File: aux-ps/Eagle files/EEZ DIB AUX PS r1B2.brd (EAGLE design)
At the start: 210 x 60 mm, 116 parts, among them IC1 AMC6821SDBQR, IC2 VIPer35L, IC3 TL431, J1 PF0030/PC, J2 1-726388-2, J3 1-726388-2, J4 1-726388-2, J5 SWEB 8094 AU/GN, Q1 BTA26-600, Q2 BTA26-600, Q3 2N7002, Q4 2N7002, Q5 BSP716NH6327XTSA1, Q6 2N7002, SW1 DF62J12S2AHQA, X1 39-28-1063, X2 39-30-1039, X3 ZL231-16KG, X4 22-23-2031, X5 22-23-2021

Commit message: r1B2 changes
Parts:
- removed LED2: LTST-C170YKT, EEZ_Lib1:LED_0805
- added R35: 1K8, rcl:R0805
- added R36: 47K, rcl:R0805
- added R37: 4K7, rcl:R0805
- C13, C19: device rcl:C1206 -> rcl:C1210
- C20: value *** -> N.C.
- C23: value 10n -> 3n3
- R11: value 2K2 -> 330R/2W; device rcl:R0805 -> rcl:R2512
- R12: value 10K -> 47K
- R13: value 470R -> 2K2
- R14, R33: value 47K -> 10K
- R15: value 10K -> 470R
- R16: value 4K7 -> 47K
- R17: value 220K -> 10K; device rcl:R1206 -> rcl:R0805
- R18: value 220K -> 4K7; device rcl:R1206 -> rcl:R0805
- R19, R21: value 120R -> 220K; device rcl:R0805 -> rcl:R1206
- R20: value 100K -> 220K; device rcl:R0805 -> rcl:R1206
- R22: value 22R -> 120R
- R23: value 120R -> 100K
- R24: value 470R -> 120R
- R25, R28: value *** -> 1K
- R26: value N.C. -> 22R
- R27: value 24K -> 120R
- R29: value 47K -> N.C.
- R30: value 47K -> 4K7
- R31: value 12K -> 10K
- R32: value 1K8 -> 47K
- R34: value 4K7 -> 6K8
- R6: value 49R9 -> 47K
- R7: value 220R -> 330R/2W; device rcl:R0805 -> rcl:R2512
- R8: value 330R/2W -> 49R9; device rcl:R2512 -> rcl:R0805
- R9: value 330R/2W -> 220R; device rcl:R2512 -> rcl:R0805
- moved R24 107.0 mm to (113.7, 54.3), turned to 270 degrees
- moved R11 99.2 mm to (137.4, 6.10), turned to 270 degrees
- moved R6 77.6 mm to (71.8, 52.2), turned to 90 degrees
- moved R14 67.4 mm to (103.8, 55.0), turned to 270 degrees
- moved R22 59.3 mm to (62.4, 38.0), turned to 90 degrees
- moved R17 58.9 mm to (49.4, 43.9)
- moved R33 58.3 mm to (65.7, 18.4), turned to 0 degrees
- moved R18 57.9 mm to (47.4, 43.9), turned to 90 degrees
- moved R34 55.2 mm to (115.3, 38.4), turned to 180 degrees
- moved R9 52.0 mm to (145.2, 58.0), turned to 180 degrees
- moved R23 50.8 mm to (110.2, 44.3), turned to 0 degrees
- moved R31 45.7 mm to (74.9, 17.1), turned to 270 degrees
- moved R19 44.3 mm to (105.3, 26.7)
- moved R12 32.0 mm to (71.8, 56.1), turned to 90 degrees
- moved R27 21.2 mm to (62.4, 29.1), turned to 270 degrees
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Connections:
- removed net N$10: LED2.C, R24.1
- removed net N$63: C3.1, C4.1, D1.C, L1.1, R12.2, X4.1
- new net +12V_FAN: C3.1, C4.1, D1.C, L1.1, R14.2, X4.1
- net +12V_REC: now also R22.1, R25.1; no longer R19.1
- net +3V3: now also R13.1; no longer R11.1
- net +5V: now also R16.1, R30.2; no longer LED2.A, R14.1, R27.2
- net +5V_REC: now also R27.1; no longer R23.1
- net 0V: now also R34.1, R35.2, R36.2; no longer R31.1, R32.2, R33.2
- net AC_N_OUT: now also R11.1; no longer R9.1
- net AC_OUT_L: now also R7.2; no longer R8.2
- net AUX: now also R29.2; no longer R26.2
- net AUX_OUT: now also R26.2; no longer R22.2
- net AUX_REC: now also R24.1, R26.1; no longer R21.1, R22.1
- net DC_BUS: now also R19.1, R20.1, R21.1; no longer R17.1, R18.1
- net FAN_SENSE: now also R14.1, R17.2; no longer R12.1, R15.2
- net FB1: now also R31.2; no longer R28.2
- net GND: now also R12.1, R18.2, R25.2, R37.1, R6.1; no longer R16.2, R24.2, R34.1
- net N$12: now also R28.1; no longer R25.1
- net N$13: now also R15.2; no longer R13.2
- net N$137: now also R19.2, R20.2; no longer R17.2
- net N$14: now also R15.1; no longer R13.1
- net N$140: now also R24.2; no longer R21.2
- net N$141: now also R32.1, R34.2; no longer R26.1, R31.2
- net N$146: now also R27.2; no longer R23.2
- net N$148: now also R30.1, R33.2, R37.2; no longer R27.1, R30.2, R34.2
- net N$149: now also R33.1; no longer R30.1
- net N$152: now also R36.1; no longer R33.1
- net N$155: now also R32.2; no longer R29.2
- net N$16: now also R9.2; no longer R7.2
- net N$174: now also R8.1; no longer R6.1
- net N$2: now also R17.1, R18.1; no longer R15.1, R16.1
- net N$20: now also R23.2, R35.1; no longer R20.2, R32.1
- net N$49: now also R21.2, R23.1; no longer R18.2, R20.1
- net N$5: now also R28.2, R31.1; no longer R25.2, R28.1
- net N$58: now also R13.2; no longer R11.2
- net N$73: now also R7.1; no longer R8.1
- net N$75: now also R8.2, R9.1; no longer R6.2, R7.1
- net N$8: now also R22.2; no longer R19.2
- net N$83: now also R11.2; no longer R9.2
- net PWR_DIRECT: now also R6.2
- net PWR_DIR_OUT: now also R16.2; no longer R14.2
- net PWR_SSTART: now also R12.2
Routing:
- net GND: track 107.4 -> 57.3 mm
- net N$63: track 23.2 -> 0.00 mm, vias 1 -> 0
- net +12V_FAN: track 0.00 -> 22.6 mm, vias 0 -> 1
- net PE: track 493.3 -> 474.8 mm
- net +5V: track 256.3 -> 245.8 mm, vias 4 -> 3
- net N$14: track 78.9 -> 71.0 mm
- net AUX: track 50.2 -> 42.4 mm, vias 2 -> 1
- net AUX_OUT: track 34.8 -> 42.4 mm
- net +12V: track 67.7 -> 74.0 mm
- net AC_OUT_L: track 65.5 -> 59.4 mm
- net 0V: track 143.6 -> 138.9 mm, vias 6 -> 5
- net AC_N_OUT: track 190.9 -> 195.1 mm
- net SSCL: track 33.7 -> 30.7 mm
- net N$148: track 31.8 -> 28.8 mm, vias 2 -> 0
- net PWR_DIRECT: track 16.8 -> 19.6 mm
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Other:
- outline, holes or cut-outs redrawn
- board text added: "EEZ DIB AUX PS (10/2018 r1B2)"
- board text removed: "EEZ DIB AUX PS (09/2018 r1B1)"

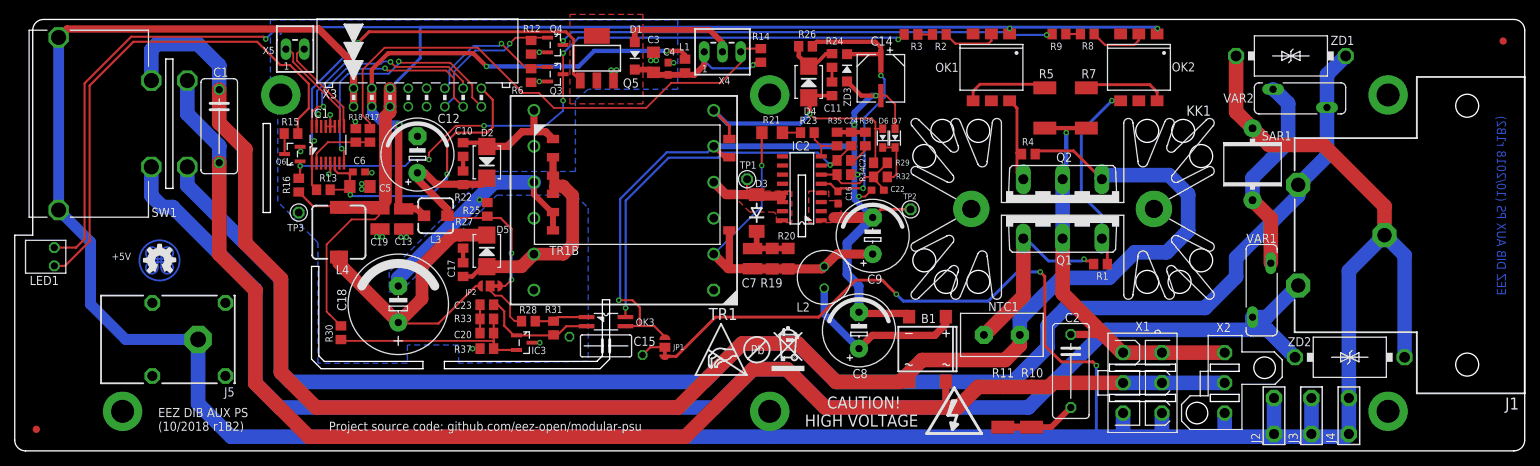
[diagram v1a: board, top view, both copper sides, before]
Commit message: PS AUX updated values for R30, C23
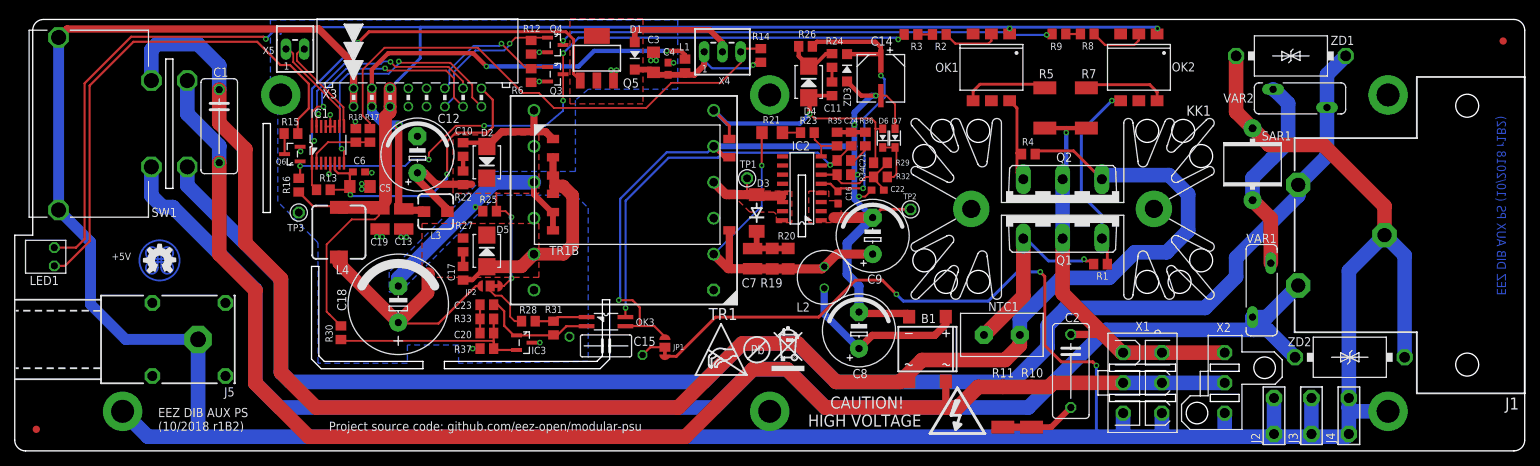
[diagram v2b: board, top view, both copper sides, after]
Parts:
- C23: value 3n3 -> 33n
- R30: value 4K7 -> 4K87
- moved L3 0.57 mm to (58.5, 33.3)
- moved C17 0.51 mm to (62.4, 24.7)
- moved R27 0.51 mm to (62.4, 28.6)
- moved R25 0.41 mm to (66.0, 33.3), turned to 180 degrees
- moved TP1 0.13 mm to (101.9, 37.9)
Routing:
- net PE: track 474.8 -> 495.2 mm, vias 4 -> 6
- net +5V_REC: track 46.7 -> 34.6 mm
- net +12V_REC: track 37.9 -> 31.2 mm
- net 5VAC: track 32.4 -> 32.9 mm
- added copper zone on layer 1, net +12V_REC
- added copper zone on layer 1, net +5V_REC

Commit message: #23, #24
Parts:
- added R38: 4K7, rcl:R0805
- C12: value 470u/25V -> UVZ1C471MPD; device EEZ_Lib1:ECAP5/10.5 -> EEZ_Lib1:ECAP3.5/8
- C3: value 10u -> 1u; device rcl:C1206 -> rcl:C0805
- C4: value 100n -> 10u; device rcl:C0603 -> rcl:C1206
- C5: value 10u -> UVZ1C471MPD; device rcl:C1206 -> EEZ_Lib1:ECAP3.5/8
- R19: value 220K -> 2K2; device rcl:R1206 -> rcl:R0805
- R22: value 120R -> 220K; device rcl:R0805 -> rcl:R1206
- R23: value 100K -> 120R
- R24: value 120R -> 100K
- R25, R28: value 1K -> 120R
- R26: value 22R -> 1K
- R27: value 120R -> 22R
- R29: value N.C. -> 1K
- R30: value 4K87 -> N.C.
- R31: value 10K -> 4K87
- R32: value 47K -> 10K
- R33: value 10K -> 47K
- R34: value 6K8 -> 10K
- R35: value 1K8 -> 6K8
- R36: value 47K -> 1K8
- R37: value 4K7 -> 47K
- moved R30 78.7 mm to (120.4, 40.1), turned to 180 degrees
- moved R37 59.2 mm to (117.2, 43.4), turned to 90 degrees
- moved R19 59.1 mm to (48.0, 41.0), turned to 180 degrees
- moved R33 58.2 mm to (120.4, 38.1)
- moved R27 55.1 mm to (110.0, 56.3), turned to 0 degrees
- moved C5 54.6 mm to (99.8, 54.3), turned to 90 degrees
- moved R29 53.7 mm to (71.4, 18.0), turned to 0 degrees
- moved R34 53.6 mm to (65.7, 18.4), turned to 0 degrees
- moved R25 52.0 mm to (113.7, 54.3), turned to 270 degrees
- moved R32 50.1 mm to (74.9, 17.1), turned to 270 degrees
- moved R26 49.6 mm to (66.0, 33.3), turned to 180 degrees
- moved R23 48.3 mm to (62.4, 38.0), turned to 90 degrees
- moved C4 46.2 mm to (47.6, 36.8), turned to 180 degrees
- moved R22 43.4 mm to (105.3, 44.3), turned to 0 degrees
- moved R31 29.6 mm to (45.4, 16.4), turned to 90 degrees
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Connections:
- new net N$3: IC1.7, R19.1
- net +12V_FAN: now also C5.+; no longer C4.1
- net +12V_REC: now also R23.1, R26.1; no longer R22.1, R25.1
- net +3V3: now also C4.2, R19.2; no longer C5.2
- net +5V: now also R31.2; no longer R30.2
- net +5V_REC: now also R28.1; no longer R27.1
- net 0V: now also R35.1, R37.2; no longer R34.1, R35.2
- net AUX: now also R30.2; no longer R29.2
- net AUX_OUT: now also R27.2; no longer R26.2
- net AUX_REC: now also R25.1, R27.1; no longer R24.1, R26.1
- net DC_BUS: now also R22.1; no longer R19.1
- net FAN_OUT: now also C5.-
- net FB1: now also R32.2; no longer R31.2
- net GND: now also C4.1, R26.2, R38.1; no longer C4.2, C5.1, R25.2, R37.1
- net N$12: now also R29.1; no longer R28.1
- net N$137: now also R21.2; no longer R19.2
- net N$140: now also R25.2; no longer R24.2
- net N$141: now also R30.1, R33.1, R35.2; no longer R29.1, R32.1, R34.2
- net N$146: now also R28.2; no longer R27.2
- net N$148: now also R31.1, R34.2, R38.2; no longer R30.1, R33.2, R37.2
- net N$149: now also R34.1; no longer R33.1
- net N$152: now also R37.1; no longer R36.1
- net N$155: now also R33.2; no longer R32.2
- net N$20: now also R24.2, R36.1; no longer R23.2, R35.1
- net N$49: now also R22.2, R24.1; no longer R21.2, R23.1
- net N$5: now also R29.2, R32.1; no longer R28.2, R31.1
- net N$8: now also R23.2; no longer R22.2
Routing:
- net GND: track 57.6 -> 203.6 mm, vias 21 -> 18
- net FAN_SENSE: track 73.0 -> 56.6 mm, vias 0 -> 1
- net +12V_FAN: track 22.6 -> 34.7 mm
- net N$3: track 0.00 -> 7.82 mm, vias 0 -> 2
- net FAN_OUT: track 16.0 -> 23.6 mm
- net +12V: track 73.9 -> 68.6 mm
- net VIPER_D: track 12.7 -> 9.07 mm
- net N$138: track 54.0 -> 51.3 mm
- net PWR_DIRECT: track 19.6 -> 16.9 mm
- net 0V: track 138.9 -> 136.7 mm
- net PWR_SSTART: track 20.8 -> 22.8 mm
- net N$13: track 2.89 -> 4.05 mm
- net N$20: track 5.92 -> 4.78 mm
- net N$14: track 71.0 -> 70.0 mm
- net +3V3: track 42.7 -> 43.7 mm
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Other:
- board text added: "EEZ DIB AUX PS (11/2018 r1B2)"
- board text removed: "+5V"
- board text removed: "EEZ DIB AUX PS (10/2018 r1B2)"

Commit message: first commit of DCP505 power board
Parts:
- removed R38: 4K7, rcl:R0805
- removed TP3: (no value), EEZ_Lib1:PCB_SHIELD_TAB
- R10, R5: value 330R/2W -> 47K; device rcl:R2512 -> rcl:R0805
- R11: value 330R/2W -> 2K2; device rcl:R2512 -> rcl:R0805
- R12, R33: value 47K -> 10K
- R13: value 2K2 -> 470R
- R14, R32: value 10K -> 47K
- R15: value 470R -> 10K
- R16, R37: value 47K -> 4K7
- R17: value 10K -> 2K2
- R18: value 4K7 -> 220K; device rcl:R0805 -> rcl:R1206
- R19: value 2K2 -> 220K; device rcl:R0805 -> rcl:R1206
- R2: value 49R9 -> 270R
- R20: value 220K -> 100K
- R21, R22: value 220K -> 120R; device rcl:R1206 -> rcl:R0805
- R23, R28: value 120R -> 1K
- R24: device rcl:R0805 -> rcl:R1206
- R25: value 120R -> 22R
- R26: value 1K -> 100K; device rcl:R0805 -> rcl:R1206
- R27: value 22R -> 120R
- R29: value 1K -> N.C.
- R3: value 220R -> 2K2
- R30: value N.C. -> 4K87
- R31: value 4K87 -> 10K
- R34: value 10K -> 6K8
- R35: value 6K8 -> 1K8
- R36: value 1K8 -> 47K
- R4: value 2K2 -> 330R/2W; device rcl:R0805 -> rcl:R2512
- R6: value 47K -> 330R/2W; device rcl:R0805 -> rcl:R2512
- R7: value 330R/2W -> 270R; device rcl:R2512 -> rcl:R0805
- R8: value 49R9 -> 330R/2W; device rcl:R0805 -> rcl:R2512
- R9: value 220R -> 330R/2W; device rcl:R0805 -> rcl:R2512
- moved R11 99.6 mm to (42.5, 36.3), turned to 180 degrees
- moved R10 85.7 mm to (71.8, 56.1), turned to 90 degrees
- moved TP2 85.2 mm to (39.4, 32.3)
- moved R30 78.7 mm to (45.4, 16.4), turned to 90 degrees
- moved R6 77.7 mm to (149.4, 47.7), turned to 270 degrees
- moved R5 71.6 mm to (71.8, 52.2), turned to 90 degrees
- moved R19 61.2 mm to (107.6, 26.7), turned to 90 degrees
- moved R18 60.8 mm to (105.3, 26.7)
- moved R37 59.2 mm to (65.7, 14.2), turned to 0 degrees
- moved R33 58.2 mm to (65.7, 18.4)
- moved R27 55.1 mm to (62.4, 28.6), turned to 270 degrees
- moved R29 53.7 mm to (120.4, 40.1), turned to 180 degrees
- moved R34 53.6 mm to (115.3, 38.4), turned to 180 degrees
- moved R9 52.5 mm to (137.4, 6.10), turned to 270 degrees
- moved R8 52.5 mm to (141.4, 6.10), turned to 270 degrees
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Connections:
- removed net N$10 (its old number): R2.2, R3.1
- removed net N$75: OK2.2, R8.1
- new net N$11: R24.2, R26.1
- net +12V_FAN: now also R12.2; no longer R14.2
- net +12V_REC: now also R21.1; no longer R26.1
- net +3V3: now also R11.1, R17.2; no longer R13.1, R19.2
- net +5V: now also R14.1, R30.2; no longer R16.1, R31.2
- net +5V_REC: now also R27.1; no longer R28.1
- net 0V: now also R34.1, R35.2, TP1.1; no longer R35.1, R37.2, TP2.1
- net AC_L_OUT: now also R3.2; no longer R4.2
- net AC_N_OUT: now also R8.1, R9.1; no longer R10.1, R11.1
- net AC_OUT_L: now also R4.2, R6.2; no longer R5.2, R7.2
- net AUX: now also R29.2; no longer R30.2
- net AUX_OUT: now also R25.2; no longer R27.2
- net AUX_REC: now also R22.1; no longer R27.1
- net DC_BUS: now also R18.1, R19.1; no longer R21.1, R22.1
- net FAN_SENSE: now also R12.1, R15.2; no longer R14.1, R17.2
- net FB1: now also R31.2; no longer R32.2
- net GND: now also R10.1, R16.2, R23.2, R37.1, R5.1, TP2.1; no longer R12.1, R18.2, R26.2, R38.1, R6.1, TP3.1
- net N$12: now also R28.1; no longer R29.1
- net N$13: now also R13.2; no longer R15.2
- net N$137: now also R18.2, R19.2; no longer R20.2, R21.2
- net N$14: now also R13.1; no longer R15.1
- net N$140: now also R22.2; no longer R25.2
- net N$141: now also R29.1, R32.1, R34.2; no longer R30.1, R33.1, R35.2
- net N$146: now also R27.2; no longer R28.2
- net N$148: now also R30.1, R33.2, R37.2; no longer R31.1, R34.2, R38.2
- net N$149: now also R33.1; no longer R34.1
- net N$152: now also R36.1; no longer R37.1
- net N$155: now also R32.2; no longer R33.2
- net N$16: now also R7.2; no longer R9.2
- net N$2: now also R15.1, R16.1; no longer R17.1, R18.1
- net N$20: now also R26.2, R35.1; no longer R24.2, R36.1
- net N$3: now also R17.1; no longer R19.1
- net N$49: now also R20.2; no longer R22.2
- net N$5: now also R28.2, R31.1; no longer R29.2, R32.1
- net N$58: now also R11.2; no longer R13.2
- net N$7: now also OK2.2, R7.1; no longer R8.2, R9.1
- net N$71: now also R3.1; no longer R4.1
- net N$73: now also R6.1; no longer R7.1
- net N$76: now also R4.1; no longer R5.1
- net N$8: now also R21.2; no longer R23.2
- net N$83: now also R8.2, R9.2; no longer R10.2, R11.2
- net PWR_DIRECT: now also R5.2; no longer R6.2
- net PWR_DIR_OUT: now also R14.2, R2.2; no longer R16.2, R3.2
- net PWR_SSTART: now also R10.2; no longer R12.2
- net VIPER_D: no longer TP1.1
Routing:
- net PE: track 495.2 -> 476.7 mm, vias 6 -> 5
- net N$75: track 7.98 -> 0.00 mm
- net N$7: track 2.04 -> 7.41 mm
- net AC_N_IN: track 216.6 -> 212.2 mm
- net AC_L_OUT: track 237.3 -> 232.8 mm
- net AC_L_IN: track 203.4 -> 199.0 mm
- net PWR_DIR_OUT: track 100.2 -> 104.6 mm
- net N$16: track 69.3 -> 73.6 mm
- net AC_N_OUT: track 195.1 -> 192.0 mm
- net DC_BUS: track 48.9 -> 45.8 mm, vias 1 -> 2
- net VIPER_D: track 9.07 -> 6.54 mm
- net N$11: track 0.00 -> 2.11 mm
- net 0V: track 136.7 -> 138.8 mm, vias 5 -> 15
- net N$10 (its old number): track 2.04 -> 0.00 mm
- net N$49: track 2.52 -> 3.41 mm
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- added copper zone on layer 16, net 0V
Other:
- outline, holes or cut-outs redrawn
- board text added: "EEZ DIB AUX PS (01/2019 r1B2)"
- board text removed: "EEZ DIB AUX PS (11/2018 r1B2)"

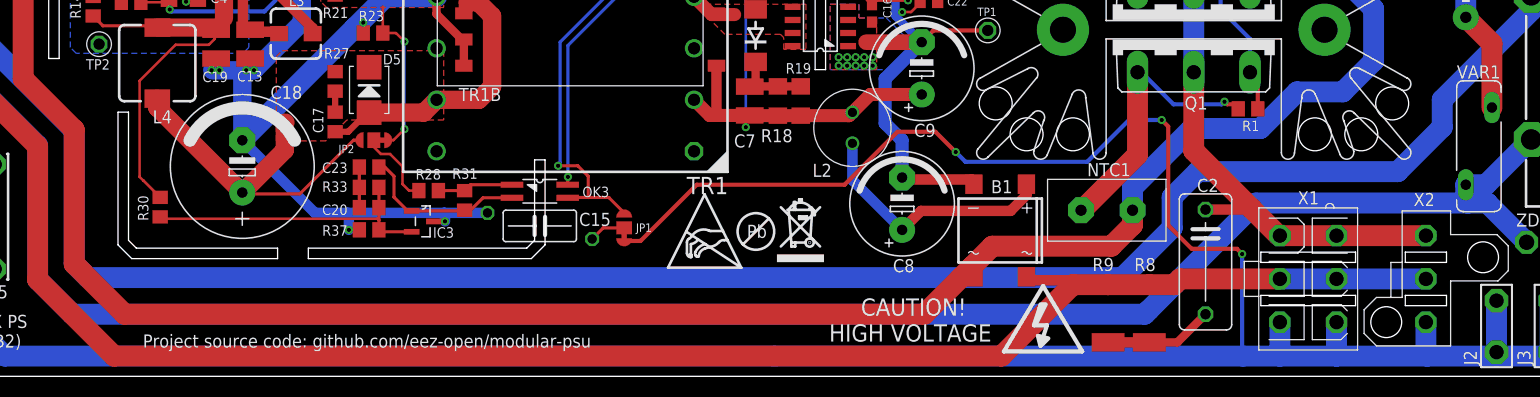
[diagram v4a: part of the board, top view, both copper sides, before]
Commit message: AUX PS C2 moved away on the PCB from X1
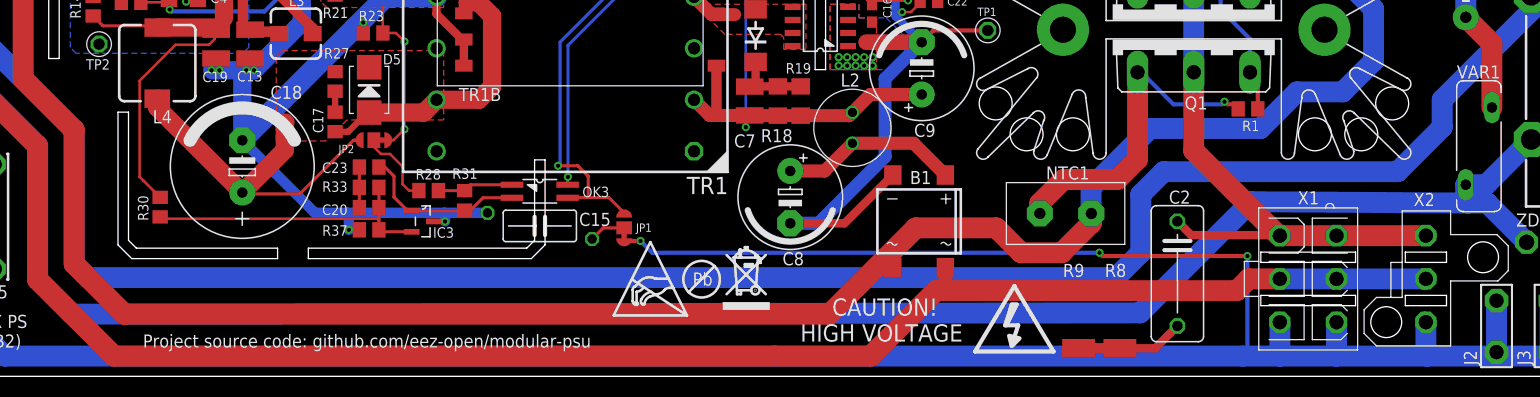
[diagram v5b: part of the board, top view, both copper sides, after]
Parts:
- moved C8 10.9 mm to (106.6, 17.4), turned to 270 degrees
- moved B1 7.92 mm to (119.1, 15.0)
- moved U$2 7.02 mm to (97.9, 9.43)
- moved U$4 7.02 mm to (89.4, 5.92)
- moved U$3 7.02 mm to (100.0, 6.45)
- moved NTC1 4.01 mm to (133.3, 15.8)
- moved C2 2.96 mm to (144.1, 9.97)
- moved R8 2.91 mm to (138.6, 5.52)
- moved R9 2.91 mm to (134.6, 5.52)
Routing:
- net PE: track 476.7 -> 459.9 mm
- net 0V: track 138.8 -> 152.5 mm
- net N$9: track 25.0 -> 17.5 mm
- net AC_OUT_L: track 60.0 -> 66.2 mm
- net N$1: track 27.2 -> 32.2 mm
- net AC_N_OUT: track 192.0 -> 189.3 mm
- net AC_L_OUT: track 232.8 -> 234.7 mm
- net AC_N_IN: track 212.2 -> 213.8 mm
